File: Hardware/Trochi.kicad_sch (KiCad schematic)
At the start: 56 parts, among them IC1 ICM-42688-P, J1 JST-SH, J2 JST-SH, J3 JST PH, J4 JST-SH, J5 JST-SH, J6 JST_SH, J7 Conn_01x09, J8 Conn_01x09, Q1 AO3401A, Q2 AO3400A, Q3 AO3400A, Q4 AO3400A, Q5 AO3400A, Q6 AO3400A, SW1 SW_SPDT, U1 ME6211C33M5, U3 YX-SMD5020

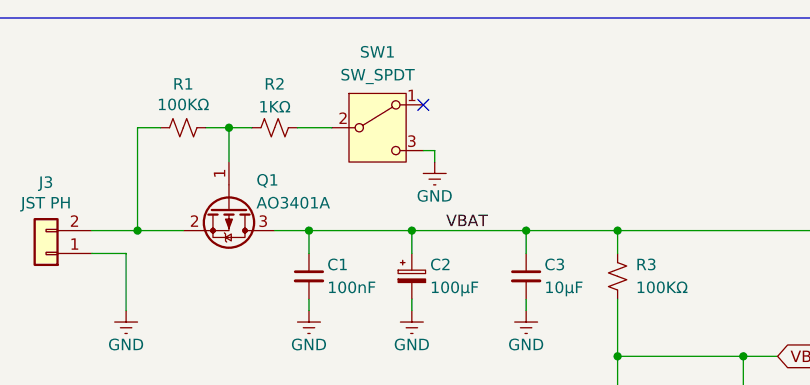
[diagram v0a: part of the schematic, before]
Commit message: feat: place bottom layer components on PCB
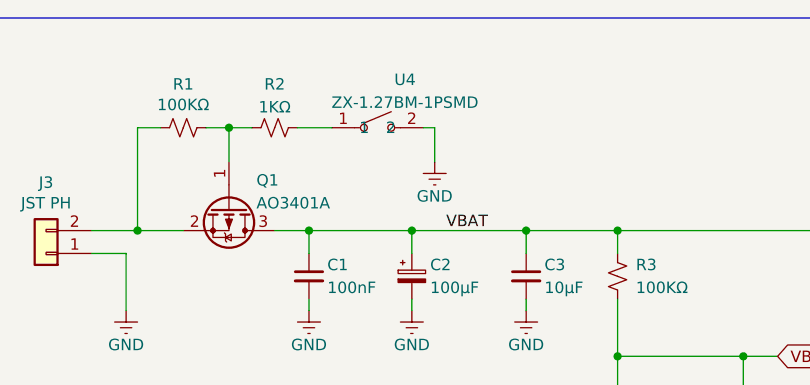
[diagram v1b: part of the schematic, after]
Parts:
- removed SW1: SW_SPDT, trochi_footprint:SW-TH_K3-1293S-E2, symbol Switch:SW_SPDT
- added U4: ZX-1.27BM-1PSMD, trochi_footprint:SW-SMD_L5.4-W2.8-LS8.2, symbol trochi_sym:ZX-1.27BM-1PSMD
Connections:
- net GND: now also U4.2
- net at R2.2: now also U4.1
- no-connect marks 6 -> 5
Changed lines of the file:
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@@
 	)
 	(no_connect
-		(at 59.69 21.59)
-	)
-	(no_connect
 		(at 124.46 161.29)
 	)
@@
 	(wire
 		(pts
-			(xy 60.96 26.67) (xy 59.69 26.67)
-		)
-		(stroke
-			(width 0)
-			(type default)
-		)
-	)
-	(wire
-		(pts
 			(xy 120.65 82.55) (xy 120.65 91.44)
 		)
@@
 	(wire
 		(pts
+			(xy 59.69 24.13) (xy 60.96 24.13)
+		)
+		(stroke
+			(width 0)
+			(type default)
+		)
+	)
+	(wire
+		(pts
 			(xy 260.35 101.6) (xy 260.35 104.14)
 		)
@@
 	(wire
 		(pts
-			(xy 60.96 27.94) (xy 60.96 26.67)
+			(xy 60.96 24.13) (xy 60.96 27.94)
 		)
 		(stroke
@@
 	)
 	(symbol
-		(lib_id "Switch:SW_SPDT")
-		(at 54.61 24.13 0)
-		(unit 1)
-		(body_style 1)
-		(exclude_from_sim no)
-		(in_bom yes)
-		(on_board yes)
-		(in_pos_files yes)
-		(dnp no)
-		(property "Reference" "SW1"
-			(at 54.61 15.748 0)
-			(show_name no)
-			(do_not_autoplace no)
-			(effects
-				(font
-					(size 1.27 1.27)
-				)
-			)
-		)
-		(property "Value" "SW_SPDT"
-			(at 54.61 18.288 0)
-			(show_name no)
-			(do_not_autoplace no)
-			(effects
-				(font
-					(size 1.27 1.27)
-				)
-			)
-		)
-		(property "Footprint" "trochi_footprint:SW-TH_K3-1293S-E2"
-			(at 54.61 24.13 0)
-			(hide yes)
-			(show_name no)
-			(do_not_autoplace no)
-			(effects
-				(font
-					(size 1.27 1.27)
-				)
-			)
-		)
-		(property "Datasheet" ""
-			(at 54.61 31.75 0)
-			(hide yes)
-			(show_name no)
-			(do_not_autoplace no)
-			(effects
-				(font
-					(size 1.27 1.27)
-				)
-			)
-		)
-		(property "Description" "Switch, single pole double throw"
-			(at 54.61 24.13 0)
-			(hide yes)
-			(show_name no)
-			(do_not_autoplace no)
-			(effects
-				(font
-					(size 1.27 1.27)
-				)
-			)
-		)
-		(property "LCSC" "https://www.lcsc.com/product-detail/C145852.html"
-			(at 54.61 24.13 0)
-			(hide yes)
-			(show_name no)
-			(do_not_autoplace no)
-			(effects
-				(font
-					(size 1.27 1.27)
-				)
-			)
-		)
-		(property "Part Number" "C145852"
-			(at 54.61 24.13 0)
-			(hide yes)
-			(show_name no)
-			(do_not_autoplace no)
-			(effects
-				(font
-					(size 1.27 1.27)
-				)
-			)
-		)
-		(pin "3"
-		)
-		(pin "1"
-		)
-		(pin "2"
-		)
-		(instances
-			(project "Trochi"
-				(path "/a5119cab-c33d-484e-b542-18705d0dc8d0"
-					(reference "SW1")
-					(unit 1)
-				)
-			)
-		)
-	)
-	(symbol
 		(lib_id "Device:C_Small")
 		(at 46.99 40.64 0)
@@
 					(unit 1)
 				)
+			)
+		)
+	)
+	(symbol
+		(lib_id "trochi_sym:ZX-1.27BM-1PSMD")
+		(at 54.61 22.86 0)
+		(unit 1)
+		(body_style 1)
+		(exclude_from_sim no)
+		(in_bom yes)
+		(on_board yes)
+		(in_pos_files yes)
+		(dnp no)
+		(property "Reference" "U4"
+			(at 57.658 18.796 0)
+			(show_name no)
+			(do_not_autoplace no)
+			(effects
+				(font
+					(size 1.27 1.27)
+				)
+			)
+		)
+		(property "Value" "ZX-1.27BM-1PSMD"
+			(at 57.658 21.336 0)
+			(show_name no)
+			(do_not_autoplace no)
+			(effects
+				(font
+					(size 1.27 1.27)
+				)
+			)
+		)
+		(property "Footprint" "trochi_footprint:SW-SMD_L5.4-W2.8-LS8.2"
+			(at 54.61 31.75 0)
+			(hide yes)
+			(show_name no)
+			(do_not_autoplace no)
+			(effects
+				(font
+					(size 1.27 1.27)
+				)
+			)
+		)
+		(property "Datasheet" "https://www.lcsc.com/datasheet/C7527751.pdf"
+			(at 54.61 34.29 0)
+			(hide yes)
+			(show_name no)
+			(do_not_autoplace no)
+			(effects
+				(font
+					(size 1.27 1.27)
+				)
+			)
+		)
+		(property "Description" ""
+			(at 54.61 22.86 0)
+			(hide yes)
+			(show_name no)
+			(do_not_autoplace no)
+			(effects
+				(font
+					(size 1.27 1.27)
+				)
+			)
+		)
+		(property "Manufacturer" "Megastar(兆星)"
+			(at 54.61 36.83 0)
+			(hide yes)
+			(show_name no)
+			(do_not_autoplace no)
+			(effects
+				(font
+					(size 1.27 1.27)
+				)
+			)
+		)
+		(property "MPN" "ZX-1.27BM-1PSMD"
+			(at 54.61 39.37 0)
+			(hide yes)
+			(show_name no)
+			(do_not_autoplace no)
+			(effects
+				(font
+					(size 1.27 1.27)
+				)
+			)
+		)
+		(property "LCSC Part" "C7527751"
+			(at 54.61 41.91 0)
+			(hide yes)
+			(show_name no)
+			(do_not_autoplace no)
+			(effects
+				(font
+					(size 1.27 1.27)
+				)
+			)
+		)
+		(pin "2"
+		)
+		(pin "1"
+		)
+		(instances
+			(project "Trochi"
+				(path "/a5119cab-c33d-484e-b542-18705d0dc8d0"
+					(reference "U4")
+					(unit 1)
+				)

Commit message: fix: update C2 footprint
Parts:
- C2: footprint Capacitor_SMD:C_1206_3216Metric -> Capacitor_SMD:C_0805_2012Metric
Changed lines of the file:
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@@
 			)
 		)
-		(property "Footprint" "Capacitor_SMD:C_1206_3216Metric"
+		(property "Footprint" "Capacitor_SMD:C_0805_2012Metric"
 			(at 58.42 40.64 0)
 			(hide yes)

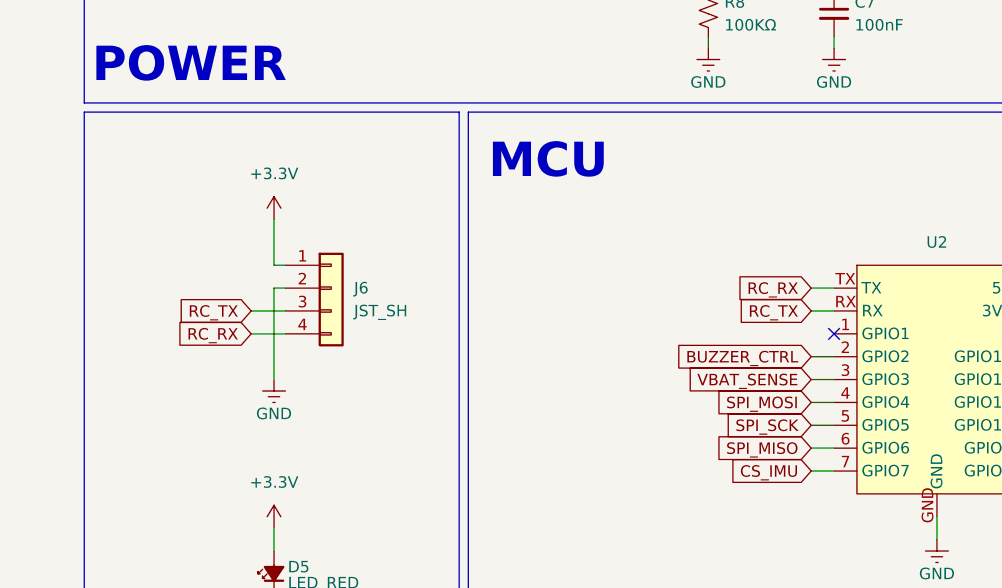
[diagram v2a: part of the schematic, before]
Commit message: feat: remove ELRS support and connector from schematic
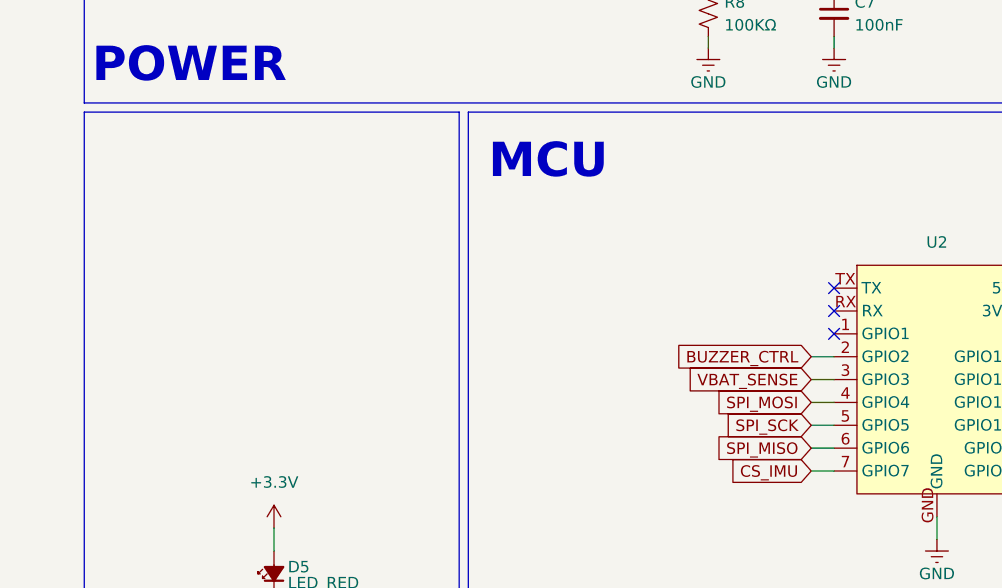
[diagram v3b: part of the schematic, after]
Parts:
- removed J6: JST_SH, trochi_footprint:CONN-SMD_4P-P1.00_SM04B-SRSS-TB-LF-SN, symbol Connector_Generic:Conn_01x04
- C2: footprint Capacitor_SMD:C_0805_2012Metric -> Capacitor_SMD:C_1206_3216Metric
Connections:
- net RC_RX: no longer names the net of U2.TX
- net RC_TX: no longer names the net of U2.RX
- no-connect marks 5 -> 7

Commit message: feat: remove power switch from schematic
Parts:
- removed D6: SS14, Diode_SMD:D_SMA, symbol Device:D_Schottky_Small
- removed Q1: AO3401A, Package_TO_SOT_SMD:SOT-23, symbol Transistor_FET:AO3401A
- removed R1: 100KΩ, Resistor_SMD:R_0402_1005Metric, symbol Device:R_Small_US
- removed R2: 1KΩ, Resistor_SMD:R_0402_1005Metric, symbol Device:R_Small_US
- removed U4: ZX-1.27BM-1PSMD, trochi_footprint:SW-SMD_L5.4-W2.8-LS8.2, symbol trochi_sym:ZX-1.27BM-1PSMD
- added D7: 1N5819W, Diode_SMD:D_SOD-123, symbol Device:D_Schottky_Small
- D1, D2, D3: value SS14 -> 1N5819W; footprint Diode_SMD:D_SMA -> Diode_SMD:D_SOD-123
- D4: value SS14 -> 1N5819W; footprint Diode_SMD:D_SMA -> Diode_SMD:D_SOD-123; LCSC (none) -> https://www.lcsc.com/product-detail/C2480.html; Part Number (none) -> C2480
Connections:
- net VBAT: now also J3.2 (Pin_2), D7.1 (K)
- net at J5.1 (Pin_1), Q5.3 (D): now also D3.2 (A); no longer D4.2 (A)
- net at J2.1 (Pin_1), Q3.3 (D): now also D7.2 (A); no longer D2.2 (A)
- net at Q6.3 (D), U3.2 (-): now also D4.2 (A)
- net at J4.1 (Pin_1), Q4.3 (D): now also D2.2 (A); no longer D3.2 (A)
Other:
- moved on the sheet: C1, C2, C3, C4, C5, C6, C7, D5, J3, R13, R3, R8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

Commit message: fix: update Schottky diodes in buzzer and motor driver circuits
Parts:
- removed D7: 1N5819W, Diode_SMD:D_SOD-123, symbol Device:D_Schottky_Small
- added D6: SS14, Diode_SMD:D_SMA, symbol Device:D_Schottky_Small
- D1, D2, D3: value 1N5819W -> SS14; footprint Diode_SMD:D_SOD-123 -> Diode_SMD:D_SMA
- D4: value 1N5819W -> SS14; footprint Diode_SMD:D_SOD-123 -> Diode_SMD:D_SMA; LCSC https://www.lcsc.com/product-detail/C2480.html -> (none); Part Number C2480 -> (none)
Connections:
- net VBAT: now also D6.1 (K)
- net at J5.1 (Pin_1), Q5.3 (D): now also D4.2 (A); no longer D3.2 (A)
- net at J2.1 (Pin_1), Q3.3 (D): now also D2.2 (A)
- net at Q6.3 (D), U3.2 (-): now also D6.2 (A); no longer D4.2 (A)
- net at J4.1 (Pin_1), Q4.3 (D): now also D3.2 (A); no longer D2.2 (A)

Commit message: fix: split C2 into three capacitors totaling 22uF
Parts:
- removed D6: SS14, Diode_SMD:D_SMA, symbol Device:D_Schottky_Small
- added C2B, C2C: 100µF, Capacitor_SMD:C_1206_3216Metric, symbol Device:C_Polarized_Small
- added D7: 1N5819W, Diode_SMD:D_SOD-123, symbol Device:D_Schottky_Small
- D1, D2, D3: value SS14 -> 1N5819W; footprint Diode_SMD:D_SMA -> Diode_SMD:D_SOD-123
- D4: value SS14 -> 1N5819W; footprint Diode_SMD:D_SMA -> Diode_SMD:D_SOD-123; LCSC (none) -> https://www.lcsc.com/product-detail/C2480.html; Part Number (none) -> C2480
- renumbered C2 to C2A
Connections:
- net GND: now also C2B.2, C2C.2
- net VBAT: now also C2B.1, C2C.1, D7.1 (K)
- net at J5.1 (Pin_1), Q5.3 (D): now also D3.2 (A); no longer D4.2 (A)
- net at J2.1 (Pin_1), Q3.3 (D): now also D7.2 (A); no longer D2.2 (A)
- net at Q6.3 (D), U3.2 (-): now also D4.2 (A)
- net at J4.1 (Pin_1), Q4.3 (D): now also D2.2 (A); no longer D3.2 (A)
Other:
- moved on the sheet: C1, C2A, C3, C7, J3, R3, R8

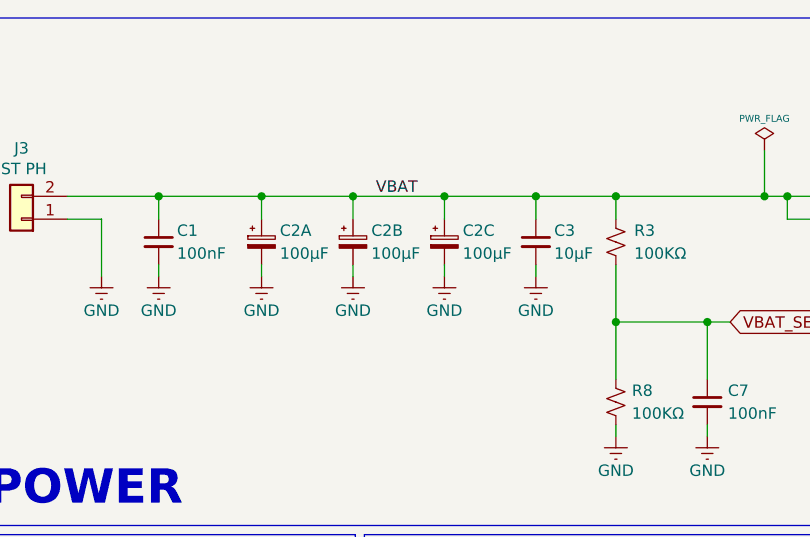
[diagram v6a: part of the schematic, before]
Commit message: fix: split C2 into three capacitors totaling 100uF
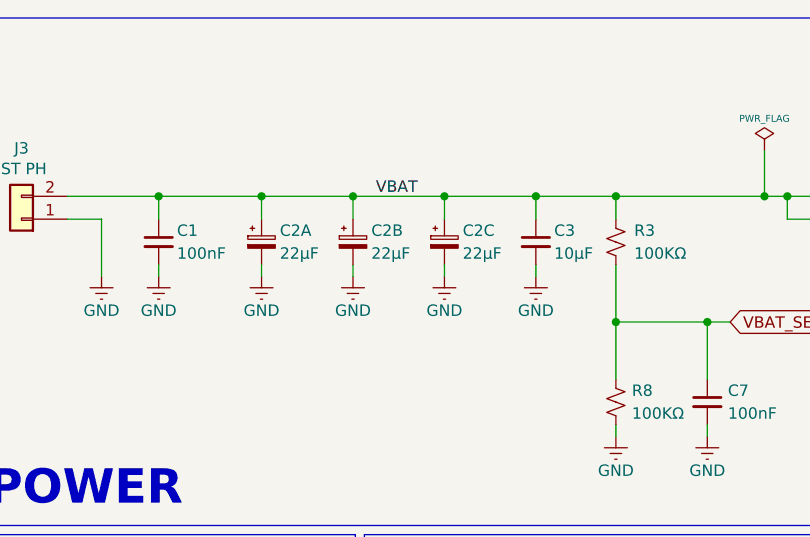
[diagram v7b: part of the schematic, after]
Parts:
- C2A, C2B, C2C: value 100µF -> 22µF
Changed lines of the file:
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@@
 			)
 		)
-		(property "Value" "100µF"
+		(property "Value" "22µF"
 			(at 55.372 38.1 0)
 			(show_name no)
@@
 			)
 		)
-		(property "Value" "100µF"
+		(property "Value" "22µF"
 			(at 45.212 38.1 0)
 			(show_name no)
@@
 			)
 		)
-		(property "Value" "100µF"
+		(property "Value" "22µF"
 			(at 65.532 38.1 0)
 			(show_name no)

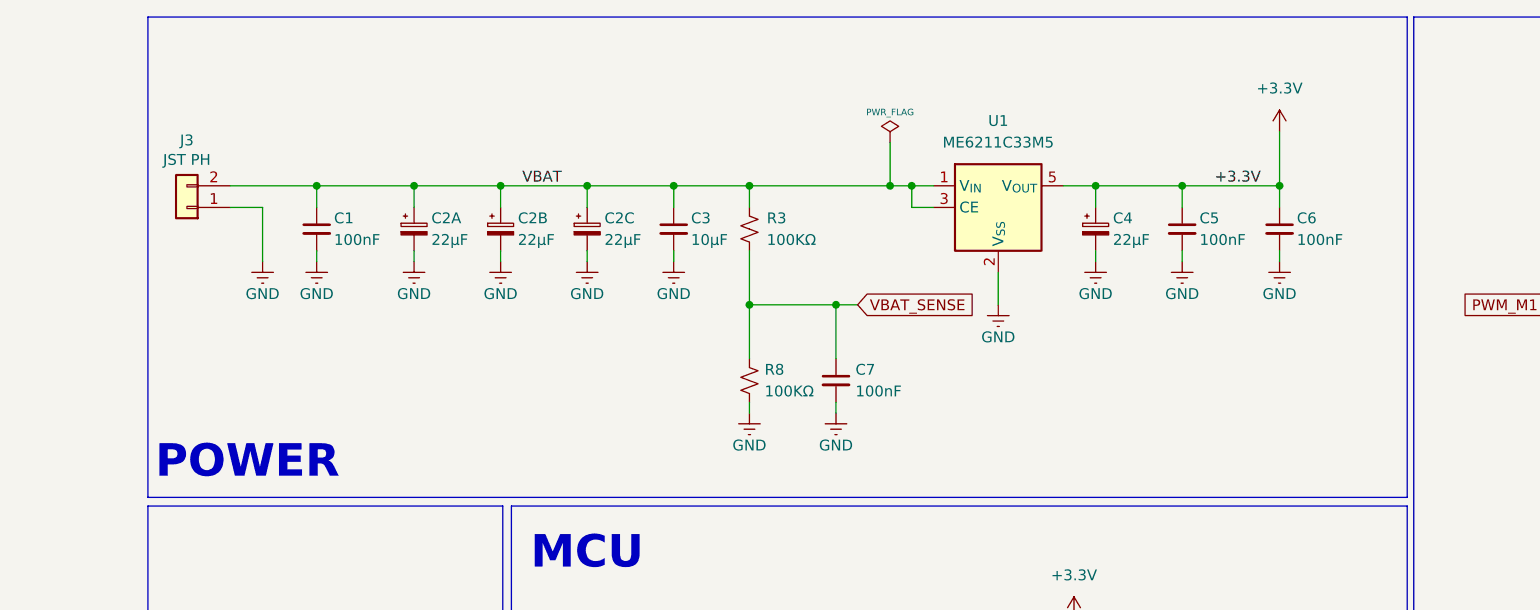
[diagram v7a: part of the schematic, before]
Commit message: chore: assign footprints to new C2 capacitors
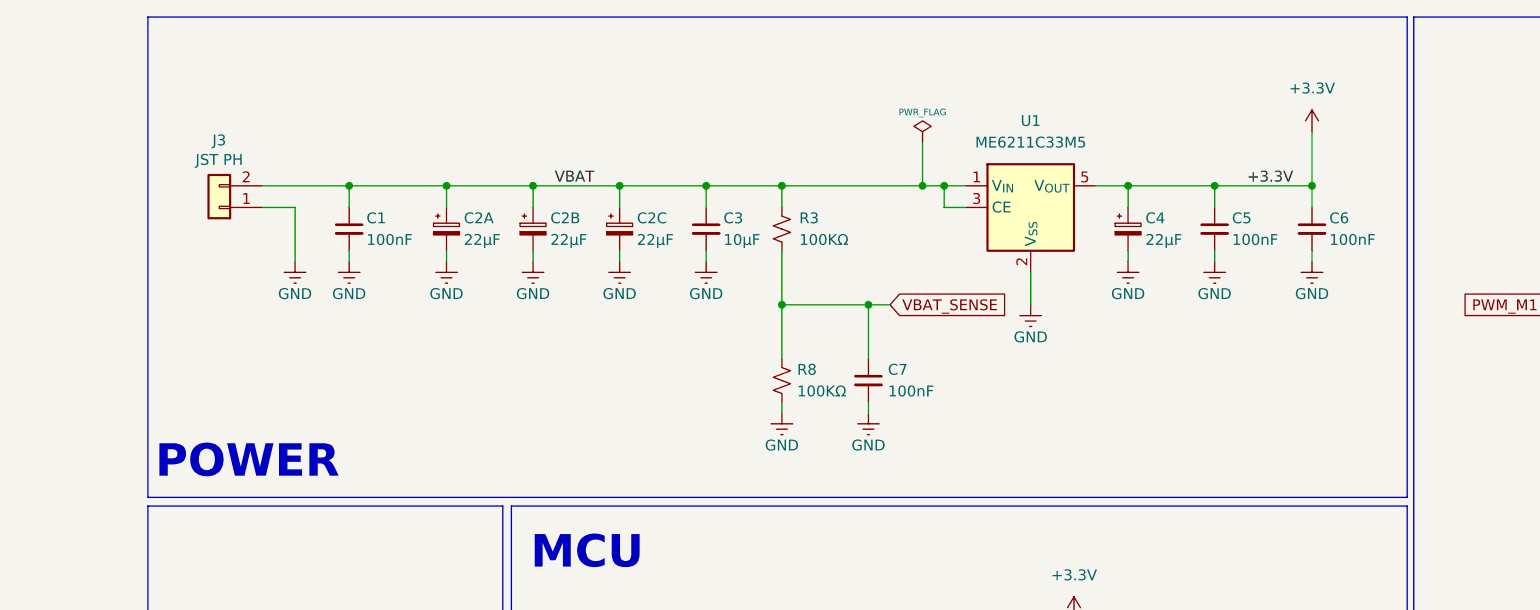
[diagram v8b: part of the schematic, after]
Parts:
- C2A, C2B, C2C: footprint Capacitor_SMD:C_1206_3216Metric -> Capacitor_SMD:C_0603_1608Metric
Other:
- moved on the sheet: C1, C2A, C2B, C2C, C3, C4, C5, C6, C7, J3, R3, R8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
